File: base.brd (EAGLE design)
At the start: 30.5 x 73.7 mm, 6 parts

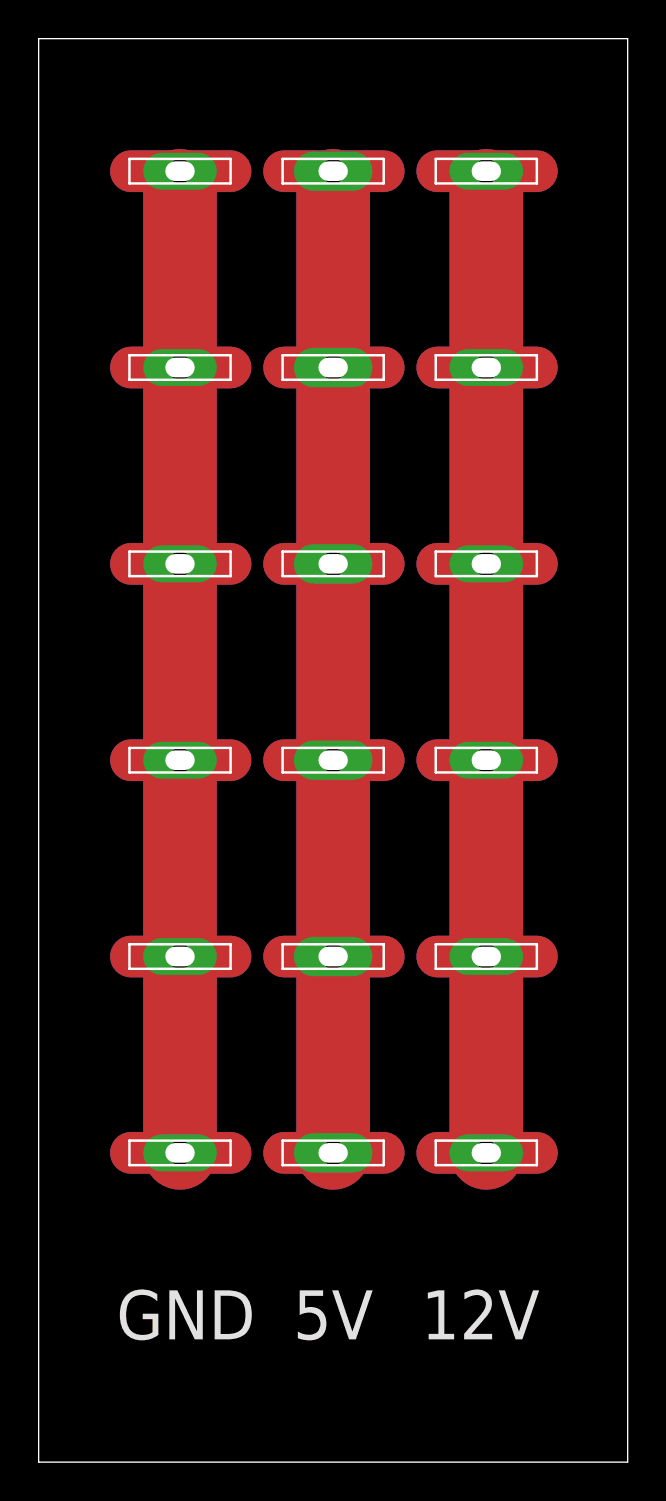
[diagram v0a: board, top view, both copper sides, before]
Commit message: made 10-mil correction to PowerPole row placements
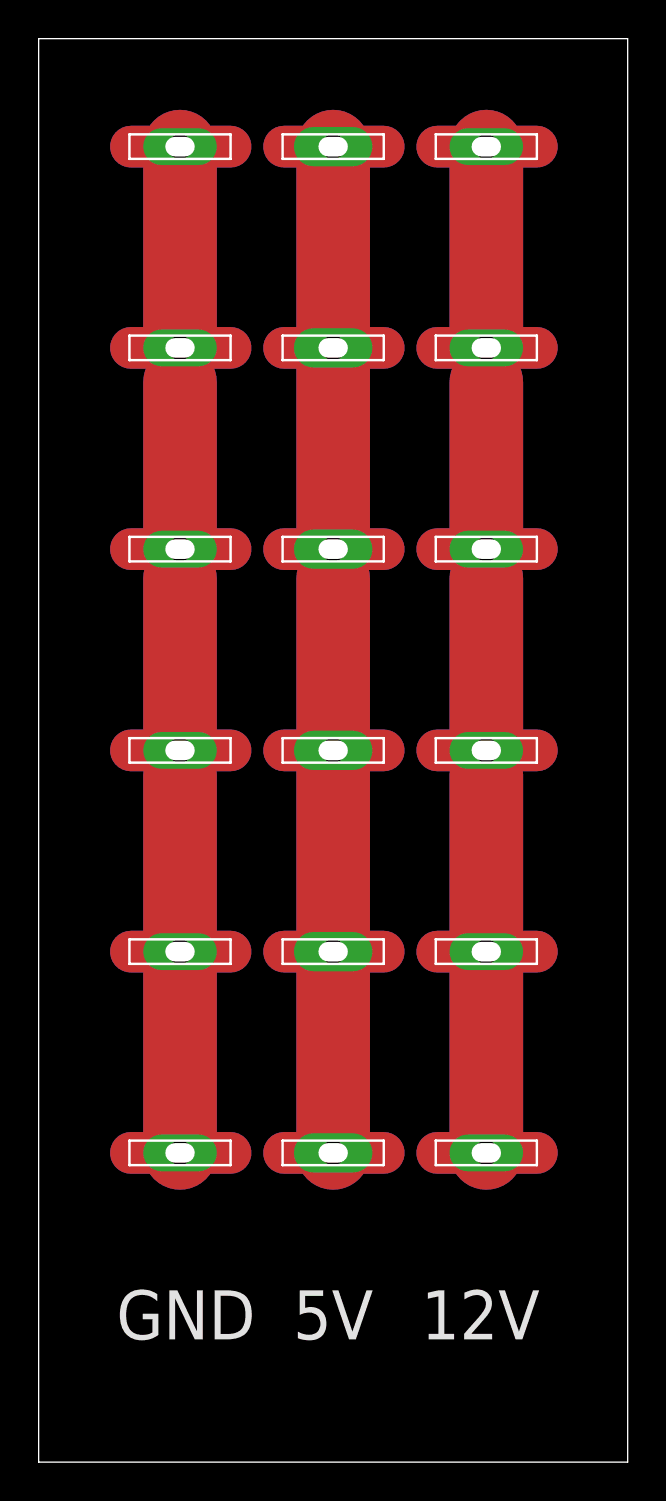
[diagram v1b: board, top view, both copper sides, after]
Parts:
- moved U$6 1.27 mm to (15.2, 68.1)
- moved U$5 1.02 mm to (15.2, 57.7)
- moved U$4 0.76 mm to (15.2, 47.2)
- moved U$3 0.51 mm to (15.2, 36.8)
- moved U$2 0.25 mm to (15.2, 26.4)
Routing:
- net 5V: track 97.0 -> 99.1 mm
- net GND: track 94.0 -> 93.0 mm
- net 12V: track 94.0 -> 93.0 mm
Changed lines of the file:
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@@
 <setting verticaltext="up"/>
 </settings>
-<grid distance="0.2" unitdist="inch" unit="inch" style="lines" multiple="1" display="yes" altdistance="0.025" altunitdist="inch" altunit="inch"/>
+<grid distance="0.1" unitdist="inch" unit="inch" style="lines" multiple="1" display="yes" altdistance="0.025" altunitdist="inch" altunit="inch"/>
 <layers>
 <layer number="1" name="Top" color="4" fill="1" visible="yes" active="yes"/>
@@
 <text x="15.24" y="7.62" size="2.54" layer="25" font="fixed" align="center">5V</text>
 <text x="22.86" y="7.62" size="2.54" layer="25" font="fixed" align="center">12V</text>
-<wire x1="15.24" y1="16.002" x2="15.24" y2="66.04" width="3.81" layer="30"/>
-<wire x1="7.3152" y1="16.002" x2="7.3152" y2="66.04" width="3.81" layer="30"/>
-<wire x1="23.1648" y1="16.002" x2="23.1648" y2="66.04" width="3.81" layer="30"/>
+<wire x1="15.24" y1="16.002" x2="15.24" y2="68.072" width="3.81" layer="30"/>
+<wire x1="7.3152" y1="16.002" x2="7.3152" y2="68.072" width="3.81" layer="30"/>
+<wire x1="23.1648" y1="16.002" x2="23.1648" y2="68.072" width="3.81" layer="30"/>
 <text x="15.24" y="10.16" size="3.556" layer="26" font="fixed" rot="MR0" align="center">NCSU</text>
 <text x="15.24" y="3.81" size="3.556" layer="26" font="fixed" rot="MR0" align="center">ARC</text>
@@
 <elements>
 <element name="U$1" library="jack" package="ARC2" value="3POLE" x="15.24" y="16.002"/>
-<element name="U$2" library="jack" package="ARC2" value="3POLE" x="15.24" y="26.162"/>
-<element name="U$3" library="jack" package="ARC2" value="3POLE" x="15.24" y="36.322"/>
-<element name="U$4" library="jack" package="ARC2" value="3POLE" x="15.24" y="46.482"/>
-<element name="U$5" library="jack" package="ARC2" value="3POLE" x="15.24" y="56.642"/>
-<element name="U$6" library="jack" package="ARC2" value="3POLE" x="15.24" y="66.802"/>
+<element name="U$2" library="jack" package="ARC2" value="3POLE" x="15.24" y="26.416"/>
+<element name="U$3" library="jack" package="ARC2" value="3POLE" x="15.24" y="36.83"/>
+<element name="U$4" library="jack" package="ARC2" value="3POLE" x="15.24" y="47.244"/>
+<element name="U$5" library="jack" package="ARC2" value="3POLE" x="15.24" y="57.658"/>
+<element name="U$6" library="jack" package="ARC2" value="3POLE" x="15.24" y="68.072"/>
 </elements>
 <signals>
@@
 <contactref element="U$1" pad="GND"/>
 <wire x1="7.3152" y1="16.002" x2="7.3152" y2="25.4" width="3.81" layer="16"/>
-<wire x1="7.3152" y1="25.4" x2="4.7752" y2="26.162" width="0" layer="19" extent="1-16"/>
-<wire x1="7.3152" y1="26.162" x2="7.3152" y2="35.56" width="3.81" layer="16"/>
-<wire x1="7.3152" y1="35.56" x2="4.7752" y2="36.322" width="0" layer="19" extent="1-16"/>
-<wire x1="7.3152" y1="36.322" x2="7.3152" y2="45.72" width="3.81" layer="16"/>
-<wire x1="7.3152" y1="45.72" x2="4.7752" y2="46.482" width="0" layer="19" extent="1-16"/>
-<wire x1="7.3152" y1="46.482" x2="7.3152" y2="55.88" width="3.81" layer="16"/>
-<wire x1="7.3152" y1="55.88" x2="4.7752" y2="56.642" width="0" layer="19" extent="1-16"/>
-<wire x1="7.3152" y1="56.642" x2="7.3152" y2="66.04" width="3.81" layer="16"/>
-<wire x1="7.3152" y1="66.04" x2="4.7752" y2="66.802" width="0" layer="19" extent="1-16"/>
+<wire x1="7.3152" y1="25.4" x2="4.7752" y2="26.416" width="0" layer="19" extent="1-16"/>
+<wire x1="7.3152" y1="26.416" x2="7.3152" y2="35.56" width="3.81" layer="16"/>
+<wire x1="7.3152" y1="35.56" x2="4.7752" y2="36.83" width="0" layer="19" extent="1-16"/>
+<wire x1="7.3152" y1="36.83" x2="7.3152" y2="45.72" width="3.81" layer="16"/>
+<wire x1="7.3152" y1="45.72" x2="4.7752" y2="47.244" width="0" layer="19" extent="1-16"/>
+<wire x1="7.3152" y1="47.244" x2="7.3152" y2="55.88" width="3.81" layer="16"/>
+<wire x1="7.3152" y1="55.88" x2="4.7752" y2="57.658" width="0" layer="19" extent="1-16"/>
+<wire x1="7.3152" y1="57.658" x2="7.3152" y2="68.072" width="3.81" layer="16"/>
+<wire x1="7.3152" y1="68.072" x2="4.7752" y2="68.072" width="0" layer="19" extent="1-16"/>
 <wire x1="7.3152" y1="16.002" x2="7.3152" y2="25.4" width="3.81" layer="1"/>
-<wire x1="7.3152" y1="26.162" x2="7.3152" y2="35.56" width="3.81" layer="1"/>
-<wire x1="7.3152" y1="36.322" x2="7.3152" y2="45.72" width="3.81" layer="1"/>
-<wire x1="7.3152" y1="46.482" x2="7.3152" y2="55.88" width="3.81" layer="1"/>
-<wire x1="7.3152" y1="56.642" x2="7.3152" y2="66.04" width="3.81" layer="1"/>
+<wire x1="7.3152" y1="26.416" x2="7.3152" y2="35.56" width="3.81" layer="1"/>
+<wire x1="7.3152" y1="36.83" x2="7.3152" y2="45.72" width="3.81" layer="1"/>
+<wire x1="7.3152" y1="47.244" x2="7.3152" y2="55.88" width="3.81" layer="1"/>
+<wire x1="7.3152" y1="57.658" x2="7.3152" y2="68.072" width="3.81" layer="1"/>
 </signal>
 <signal name="12V">
@@
 <contactref element="U$4" pad="12V"/>
 <wire x1="23.1648" y1="16.002" x2="23.1648" y2="25.4" width="3.81" layer="16"/>
-<wire x1="23.1648" y1="25.4" x2="25.781" y2="26.162" width="0" layer="19" extent="1-16"/>
-<wire x1="23.1648" y1="26.162" x2="23.1648" y2="35.56" width="3.81" layer="16"/>
-<wire x1="23.1648" y1="35.56" x2="25.781" y2="36.322" width="0" layer="19" extent="1-16"/>
-<wire x1="23.1648" y1="36.322" x2="23.1648" y2="45.72" width="3.81" layer="16"/>
-<wire x1="23.1648" y1="45.72" x2="25.781" y2="46.482" width="0" layer="19" extent="1-16"/>
-<wire x1="23.1648" y1="46.482" x2="23.1648" y2="55.88" width="3.81" layer="16"/>
-<wire x1="23.1648" y1="55.88" x2="25.781" y2="56.642" width="0" layer="19" extent="1-16"/>
-<wire x1="23.1648" y1="56.642" x2="23.1648" y2="66.04" width="3.81" layer="16"/>
-<wire x1="23.1648" y1="66.04" x2="25.781" y2="66.802" width="0" layer="19" extent="1-16"/>
+<wire x1="23.1648" y1="25.4" x2="25.781" y2="26.416" width="0" layer="19" extent="1-16"/>
+<wire x1="23.1648" y1="26.416" x2="23.1648" y2="35.56" width="3.81" layer="16"/>
+<wire x1="23.1648" y1="35.56" x2="25.781" y2="36.83" width="0" layer="19" extent="1-16"/>
+<wire x1="23.1648" y1="36.83" x2="23.1648" y2="45.72" width="3.81" layer="16"/>
+<wire x1="23.1648" y1="45.72" x2="25.781" y2="47.244" width="0" layer="19" extent="1-16"/>
+<wire x1="23.1648" y1="47.244" x2="23.1648" y2="55.88" width="3.81" layer="16"/>
+<wire x1="23.1648" y1="55.88" x2="25.781" y2="57.658" width="0" layer="19" extent="1-16"/>
+<wire x1="23.1648" y1="57.658" x2="23.1648" y2="68.072" width="3.81" layer="16"/>
+<wire x1="23.1648" y1="68.072" x2="25.781" y2="68.072" width="0" layer="19" extent="1-16"/>
 <wire x1="23.1648" y1="16.002" x2="23.1648" y2="25.4" width="3.81" layer="1"/>
-<wire x1="23.1648" y1="26.162" x2="23.1648" y2="35.56" width="3.81" layer="1"/>
-<wire x1="23.1648" y1="36.322" x2="23.1648" y2="45.72" width="3.81" layer="1"/>
-<wire x1="23.1648" y1="46.482" x2="23.1648" y2="55.88" width="3.81" layer="1"/>
-<wire x1="23.1648" y1="56.642" x2="23.1648" y2="66.04" width="3.81" layer="1"/>
+<wire x1="23.1648" y1="26.416" x2="23.1648" y2="35.56" width="3.81" layer="1"/>
+<wire x1="23.1648" y1="36.83" x2="23.1648" y2="45.72" width="3.81" layer="1"/>
+<wire x1="23.1648" y1="47.244" x2="23.1648" y2="55.88" width="3.81" layer="1"/>
+<wire x1="23.1648" y1="57.658" x2="23.1648" y2="68.072" width="3.81" layer="1"/>
 </signal>
 <signal name="5V">
@@
 <contactref element="U$1" pad="5V"/>
 <wire x1="15.24" y1="16.002" x2="15.24" y2="25.4" width="3.81" layer="16"/>
-<wire x1="15.24" y1="25.4" x2="15.24" y2="26.162" width="0" layer="19" extent="1-16"/>
-<wire x1="15.24" y1="26.162" x2="15.24" y2="36.322" width="3.81" layer="16"/>
-<wire x1="15.24" y1="36.322" x2="15.24" y2="45.72" width="3.81" layer="16"/>
-<wire x1="15.24" y1="45.72" x2="15.24" y2="46.482" width="0" layer="19" extent="1-16"/>
-<wire x1="15.24" y1="46.482" x2="15.24" y2="56.642" width="3.81" layer="16"/>
-<wire x1="15.24" y1="56.642" x2="15.24" y2="66.04" width="3.81" layer="16"/>
-<wire x1="15.24" y1="66.04" x2="15.24" y2="66.802" width="0" layer="19" extent="1-16"/>
+<wire x1="15.24" y1="25.4" x2="15.24" y2="26.416" width="0" layer="19" extent="1-16"/>
+<wire x1="15.24" y1="26.416" x2="15.24" y2="36.83" width="3.81" layer="16"/>
+<wire x1="15.24" y1="36.83" x2="15.24" y2="45.72" width="3.81" layer="16"/>
+<wire x1="15.24" y1="45.72" x2="15.24" y2="47.244" width="0" layer="19" extent="1-16"/>
+<wire x1="15.24" y1="47.244" x2="15.24" y2="57.658" width="3.81" layer="16"/>
+<wire x1="15.24" y1="57.658" x2="15.24" y2="68.072" width="3.81" layer="16"/>
+<wire x1="15.24" y1="68.072" x2="15.24" y2="68.072" width="0" layer="19" extent="1-16"/>
 <wire x1="15.24" y1="16.002" x2="15.24" y2="25.4" width="3.81" layer="1"/>
-<wire x1="15.24" y1="26.162" x2="15.24" y2="45.72" width="3.81" layer="1"/>
-<wire x1="15.24" y1="46.482" x2="15.24" y2="66.04" width="3.81" layer="1"/>
+<wire x1="15.24" y1="26.416" x2="15.24" y2="45.72" width="3.81" layer="1"/>
+<wire x1="15.24" y1="47.244" x2="15.24" y2="68.072" width="3.81" layer="1"/>
 </signal>
 </signals>

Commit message: removed air wires from GND and 12V rails (#2)
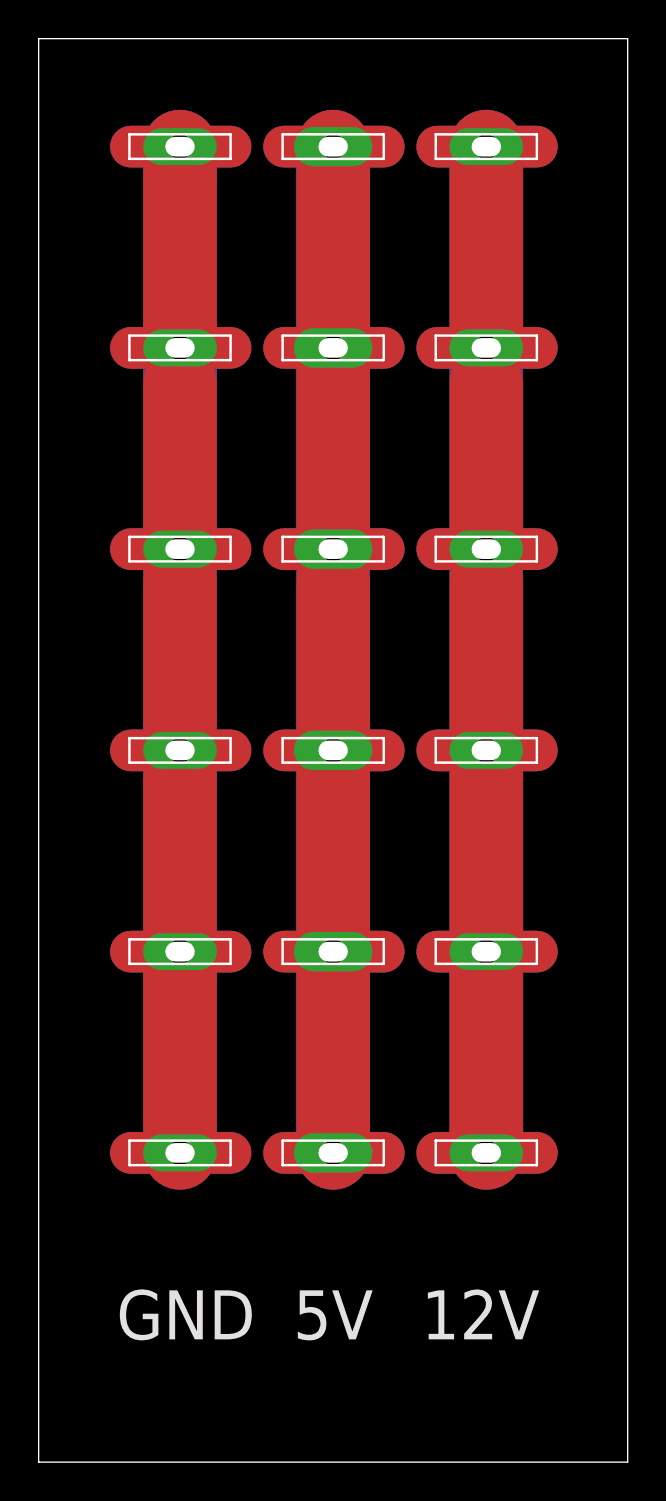
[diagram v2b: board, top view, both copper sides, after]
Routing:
- net GND: track 93.0 -> 98.6 mm
- net 12V: track 93.0 -> 98.6 mm
- net 5V: track 99.1 -> 101.6 mm

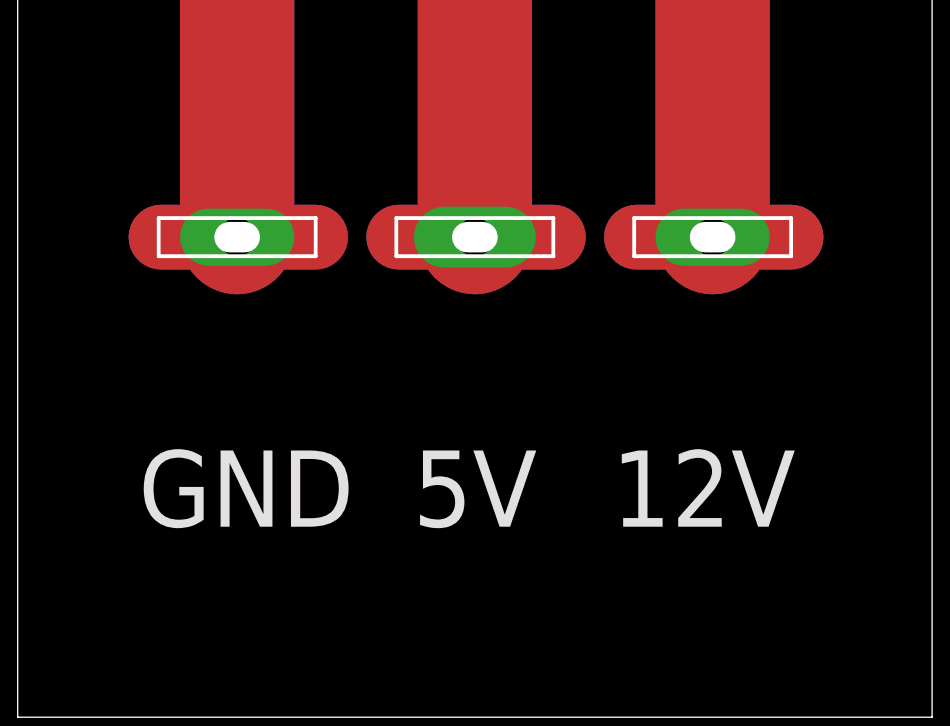
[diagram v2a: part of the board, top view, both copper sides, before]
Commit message: Extended bottom traces to solder on wires
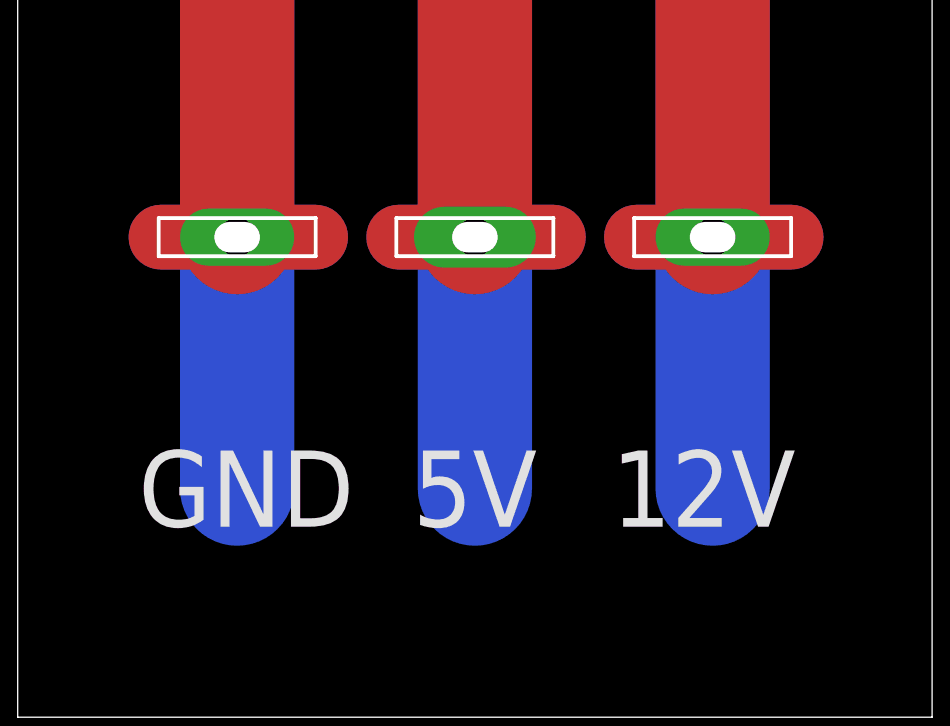
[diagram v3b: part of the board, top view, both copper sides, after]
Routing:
- net GND: track 98.6 -> 106.9 mm
- net 5V: track 101.6 -> 110.0 mm
- net 12V: track 98.6 -> 106.9 mm
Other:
- board text added: "NCSU ARC"
- board text removed: "ARC"
- board text removed: "NCSU"
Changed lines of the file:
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@@
 <text x="15.24" y="7.62" size="2.54" layer="25" font="fixed" align="center">5V</text>
 <text x="22.86" y="7.62" size="2.54" layer="25" font="fixed" align="center">12V</text>
-<wire x1="15.24" y1="16.002" x2="15.24" y2="68.072" width="3.81" layer="30"/>
-<wire x1="7.3152" y1="16.002" x2="7.3152" y2="68.072" width="3.81" layer="30"/>
-<wire x1="23.1648" y1="16.002" x2="23.1648" y2="68.072" width="3.81" layer="30"/>
-<text x="15.24" y="10.16" size="3.556" layer="26" font="fixed" rot="MR0" align="center">NCSU</text>
-<text x="15.24" y="3.81" size="3.556" layer="26" font="fixed" rot="MR0" align="center">ARC</text>
+<wire x1="15.24" y1="7.62" x2="15.24" y2="68.072" width="3.81" layer="30"/>
+<wire x1="7.3152" y1="7.62" x2="7.3152" y2="68.072" width="3.81" layer="30"/>
+<wire x1="23.1648" y1="7.62" x2="23.1648" y2="68.072" width="3.81" layer="30"/>
+<text x="15.24" y="3.81" size="3.556" layer="26" font="fixed" rot="MR0" align="center">NCSU ARC</text>
 </plain>
 <attributes>
@@
 <wire x1="7.3152" y1="36.83" x2="7.3152" y2="47.244" width="3.81" layer="16"/>
 <wire x1="7.3152" y1="47.244" x2="7.3152" y2="68.072" width="3.81" layer="16"/>
+<wire x1="7.3152" y1="7.62" x2="7.3152" y2="16.002" width="3.81" layer="16"/>
 </signal>
 <signal name="12V">
@@
 <wire x1="23.1648" y1="47.244" x2="23.1648" y2="57.658" width="3.81" layer="16"/>
 <wire x1="23.1648" y1="57.658" x2="23.1648" y2="68.072" width="3.81" layer="16"/>
+<wire x1="23.1648" y1="7.62" x2="23.1648" y2="16.002" width="3.81" layer="16"/>
 </signal>
 <signal name="5V">
@@
 <wire x1="15.24" y1="47.244" x2="15.24" y2="57.658" width="3.81" layer="16"/>
 <wire x1="15.24" y1="57.658" x2="15.24" y2="68.072" width="3.81" layer="16"/>
+<wire x1="15.24" y1="7.62" x2="15.24" y2="16.002" width="3.81" layer="16"/>
 </signal>
 </signals>
